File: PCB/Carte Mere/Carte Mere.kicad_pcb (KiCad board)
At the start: 2 copper layers, 62.2 x 23 mm, 40 parts, among them J1 Moteur, J12 Alim 6V, J13 Alim 9V, J2 Moteur, J3 01x20_Female, J4 01x20_Female, J5 IR204, J6 IR204, J7 TL1838, U1 ZXBM5210-S, U2 MC33269DR2-5.0G, U3 ZXBM5210-S, U4 LD1117S33TR_SOT223

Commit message: 1.4 Carte mere
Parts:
- moved J13 57.0 mm to (156.7, 52.5), turned to 90 degrees
- moved J12 41.0 mm to (156.7, 67.8), turned to 90 degrees
- moved J2 1.65 mm to (158.8, 58.8)
- moved J1 0.90 mm to (101.2, 58.7)
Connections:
- J12 pad 1: unconnected-(J12-Pad1) -> /Carte Mere/6V
- J12 pad 2: unconnected-(J12-Pad2) -> GND
- J13 pad 1: unconnected-(J13-Pad1) -> /Carte Mere/9V
- J13 pad 2: unconnected-(J13-Pad2) -> GND
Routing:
- net GND: track 53.0 -> 137.0 mm, vias 0 -> 3
- net /Carte Mere/3.3V: track 4.94 -> 53.7 mm, vias 0 -> 1
- net /Carte Mere/6V: track 12.7 -> 59.6 mm
- net /Carte Mere/9V: track 3.05 -> 48.1 mm
- net /Carte Mere/P2: track 0.00 -> 37.1 mm, vias 0 -> 2
- net Net-(C10-Pad1): track 0.00 -> 29.2 mm, vias 0 -> 2
- net Net-(C11-Pad1): track 0.00 -> 28.7 mm
- net /Carte Mere/P3: track 0.00 -> 27.8 mm
- net Net-(C3-Pad1): track 8.71 -> 34.4 mm, vias 0 -> 2
- net Net-(C4-Pad1): track 9.25 -> 23.2 mm
- net Net-(D3-Pad1): track 0.00 -> 6.43 mm
- net /Carte Mere/5V: track 14.7 -> 20.7 mm
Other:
- board size 62.2 x 23 mm -> 63.5 x 23 mm
- copper layers 2 -> 4
- board text added: "6V"
- board text added: "9V"
- board text added: "GND"

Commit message: 1.6
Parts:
- added J10: Conn_01x04_Male, Connector_PinHeader_2.54mm:PinHeader_1x04_P2.54mm_Vertical, F.Cu at (101.8, 74.0)
- added J11: Conn_01x04_Male, Connector_PinHeader_2.54mm:PinHeader_1x04_P2.54mm_Vertical, F.Cu at (91.5, 99.0)
- added J12: Conn_01x04_Male, Connector_PinHeader_2.54mm:PinHeader_1x04_P2.54mm_Vertical, F.Cu at (91.5, 113.8)
- added J13: Conn_01x04_Male, Connector_PinHeader_2.54mm:PinHeader_1x04_P2.54mm_Vertical, F.Cu at (91.5, 128.0)
- added R10: 10kΩ, Resistor_SMD:R_0805_2012Metric_Pad1.20x1.40mm_HandSolder, F.Cu at (96.8, 134.8)
- added R4: 500Ω, Resistor_SMD:R_0805_2012Metric_Pad1.20x1.40mm_HandSolder, F.Cu at (97.8, 100.5)
- added R5: 500Ω, Resistor_SMD:R_0805_2012Metric_Pad1.20x1.40mm_HandSolder, F.Cu at (97.8, 114.5)
- added R6: 500Ω, Resistor_SMD:R_0805_2012Metric_Pad1.20x1.40mm_HandSolder, F.Cu at (96.8, 129.2)
- added R8: 10kΩ, Resistor_SMD:R_0805_2012Metric_Pad1.20x1.40mm_HandSolder, F.Cu at (97.8, 106.0)
- added R9: 10kΩ, Resistor_SMD:R_0805_2012Metric_Pad1.20x1.40mm_HandSolder, F.Cu at (97.8, 120.2)
- added U5: TCRT5000, Library:tcrt5000, F.Cu at (117.8, 77.6)
- added U6: TCRT5000, Library:tcrt5000, F.Cu at (108.7, 103.3)
- added U7: TCRT5000, Library:tcrt5000, F.Cu at (109.0, 117.4)
- added U8: TCRT5000, Library:tcrt5000, F.Cu at (108.0, 132.1)
- moved R3 80.9 mm to (106.8, 74.8)
- moved R7 70.1 mm to (106.8, 80.2)
- renumbered J12 to J1, J13 to J2, J1 to J3, J2 to J4, J3 to J5, J4 to J6, J5 to J7, J6 to J8, J7 to J9, R9 to R3, R10 to R7
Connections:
- R3 pad 1: unconnected-(R9-Pad1) -> /Capteur/P4
- R7 pad 1: unconnected-(R10-Pad1) -> /Capteur/A0
- R7 pad 2: Net-(J11-Pad2) -> /Capteur/5V
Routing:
- net /Capteur/P4: track 0.00 -> 5.96 mm
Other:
- board size 63.5 x 23 mm -> 63.5 x 39.2 mm

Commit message: Fixed Zach's Stuff
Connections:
- U5 pad 1: (no net) -> Net-(R3-Pad2)
- U5 pad 2: (no net) -> GND
- U5 pad 4: (no net) -> GND
- U6 pad 1: (no net) -> Net-(R4-Pad2)
- U6 pad 2: (no net) -> GND
- U6 pad 3: (no net) -> GND
- U6 pad 4: (no net) -> /Capteur/A0
- U7 pad 1: (no net) -> Net-(R5-Pad2)
- U7 pad 2: (no net) -> GND
- U7 pad 4: (no net) -> GND
- U8 pad 1: (no net) -> Net-(R6-Pad2)
- U8 pad 2: (no net) -> GND
- U8 pad 4: (no net) -> GND
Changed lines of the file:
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@@
     (fp_line (start 1.36 7.59) (end 1.36 3.145) (layer "F.Fab") (width 0.1))
     (fp_line (start -4.14 7.59) (end -4.14 3.145) (layer "F.Fab") (width 0.1))
-    (pad "1" thru_hole oval (at -2.87 6.32 270) (size 1.7 1.7) (drill 1) (layers *.Cu *.Mask))
-    (pad "2" thru_hole rect (at -2.87 3.78 270) (size 1.7 1.7) (drill 1) (layers *.Cu *.Mask))
+    (pad "1" thru_hole oval (at -2.87 6.32 270) (size 1.7 1.7) (drill 1) (layers *.Cu *.Mask)
+      (net 76 "Net-(R6-Pad2)"))
+    (pad "2" thru_hole rect (at -2.87 3.78 270) (size 1.7 1.7) (drill 1) (layers *.Cu *.Mask)
+      (net 2 "GND"))
     (pad "3" thru_hole oval (at 2.63 6.32 270) (size 1.7 1.7) (drill 1) (layers *.Cu *.Mask))
-    (pad "4" thru_hole rect (at 2.63 3.78 270) (size 1.7 1.7) (drill 1) (layers *.Cu *.Mask))
+    (pad "4" thru_hole rect (at 2.63 3.78 270) (size 1.7 1.7) (drill 1) (layers *.Cu *.Mask)
+      (net 2 "GND"))
   )
   (footprint "Library:tcrt5000" (layer "F.Cu")
@@
     (fp_line (start -3.505 2.51) (end -1.6 2.51) (layer "F.Fab") (width 0.1))
     (fp_line (start 3.9 7.59) (end 1.36 7.59) (layer "F.Fab") (width 0.1))
-    (pad "1" thru_hole oval (at -2.87 6.32 270) (size 1.7 1.7) (drill 1) (layers *.Cu *.Mask))
-    (pad "2" thru_hole rect (at -2.87 3.78 270) (size 1.7 1.7) (drill 1) (layers *.Cu *.Mask))
+    (pad "1" thru_hole oval (at -2.87 6.32 270) (size 1.7 1.7) (drill 1) (layers *.Cu *.Mask)
+      (net 32 "Net-(R3-Pad2)"))
+    (pad "2" thru_hole rect (at -2.87 3.78 270) (size 1.7 1.7) (drill 1) (layers *.Cu *.Mask)
+      (net 2 "GND"))
     (pad "3" thru_hole oval (at 2.63 6.32 270) (size 1.7 1.7) (drill 1) (layers *.Cu *.Mask))
-    (pad "4" thru_hole rect (at 2.63 3.78 270) (size 1.7 1.7) (drill 1) (layers *.Cu *.Mask))
+    (pad "4" thru_hole rect (at 2.63 3.78 270) (size 1.7 1.7) (drill 1) (layers *.Cu *.Mask)
+      (net 2 "GND"))
   )
   (footprint "Resistor_SMD:R_0805_2012Metric_Pad1.20x1.40mm_HandSolder" (layer "F.Cu")
@@
     (fp_line (start -1.6 7.59) (end -4.14 7.59) (layer "F.Fab") (width 0.1))
     (fp_line (start 1.36 7.59) (end 1.36 3.145) (layer "F.Fab") (width 0.1))
-    (pad "1" thru_hole oval (at -2.87 6.32 270) (size 1.7 1.7) (drill 1) (layers *.Cu *.Mask))
-    (pad "2" thru_hole rect (at -2.87 3.78 270) (size 1.7 1.7) (drill 1) (layers *.Cu *.Mask))
-    (pad "3" thru_hole oval (at 2.63 6.32 270) (size 1.7 1.7) (drill 1) (layers *.Cu *.Mask))
-    (pad "4" thru_hole rect (at 2.63 3.78 270) (size 1.7 1.7) (drill 1) (layers *.Cu *.Mask))
+    (pad "1" thru_hole oval (at -2.87 6.32 270) (size 1.7 1.7) (drill 1) (layers *.Cu *.Mask)
+      (net 34 "Net-(R4-Pad2)"))
+    (pad "2" thru_hole rect (at -2.87 3.78 270) (size 1.7 1.7) (drill 1) (layers *.Cu *.Mask)
+      (net 2 "GND"))
+    (pad "3" thru_hole rect (at 2.63 3.78 270) (size 1.7 1.7) (drill 1) (layers *.Cu *.Mask)
+      (net 2 "GND"))
+    (pad "4" thru_hole oval (at 2.63 6.32 270) (size 1.7 1.7) (drill 1) (layers *.Cu *.Mask)
+      (net 67 "/Capteur/A0"))
   )
   (footprint "Resistor_SMD:R_0805_2012Metric_Pad1.20x1.40mm_HandSolder" (layer "F.Cu")
@@
     (fp_line (start -4.14 3.145) (end -3.505 2.51) (layer "F.Fab") (width 0.1))
     (fp_line (start -4.14 7.59) (end -4.14 3.145) (layer "F.Fab") (width 0.1))
-    (pad "1" thru_hole oval (at -2.87 6.32 270) (size 1.7 1.7) (drill 1) (layers *.Cu *.Mask))
-    (pad "2" thru_hole rect (at -2.87 3.78 270) (size 1.7 1.7) (drill 1) (layers *.Cu *.Mask))
+    (pad "1" thru_hole oval (at -2.87 6.32 270) (size 1.7 1.7) (drill 1) (layers *.Cu *.Mask)
+      (net 66 "Net-(R5-Pad2)"))
+    (pad "2" thru_hole rect (at -2.87 3.78 270) (size 1.7 1.7) (drill 1) (layers *.Cu *.Mask)
+      (net 2 "GND"))
     (pad "3" thru_hole oval (at 2.63 6.32 270) (size 1.7 1.7) (drill 1) (layers *.Cu *.Mask))
-    (pad "4" thru_hole rect (at 2.63 3.78 270) (size 1.7 1.7) (drill 1) (layers *.Cu *.Mask))
+    (pad "4" thru_hole rect (at 2.63 3.78 270) (size 1.7 1.7) (drill 1) (layers *.Cu *.Mask)
+      (net 2 "GND"))
   )
   (footprint "Resistor_SMD:R_0805_2012Metric_Pad1.20x1.40mm_HandSolder" (layer "F.Cu")

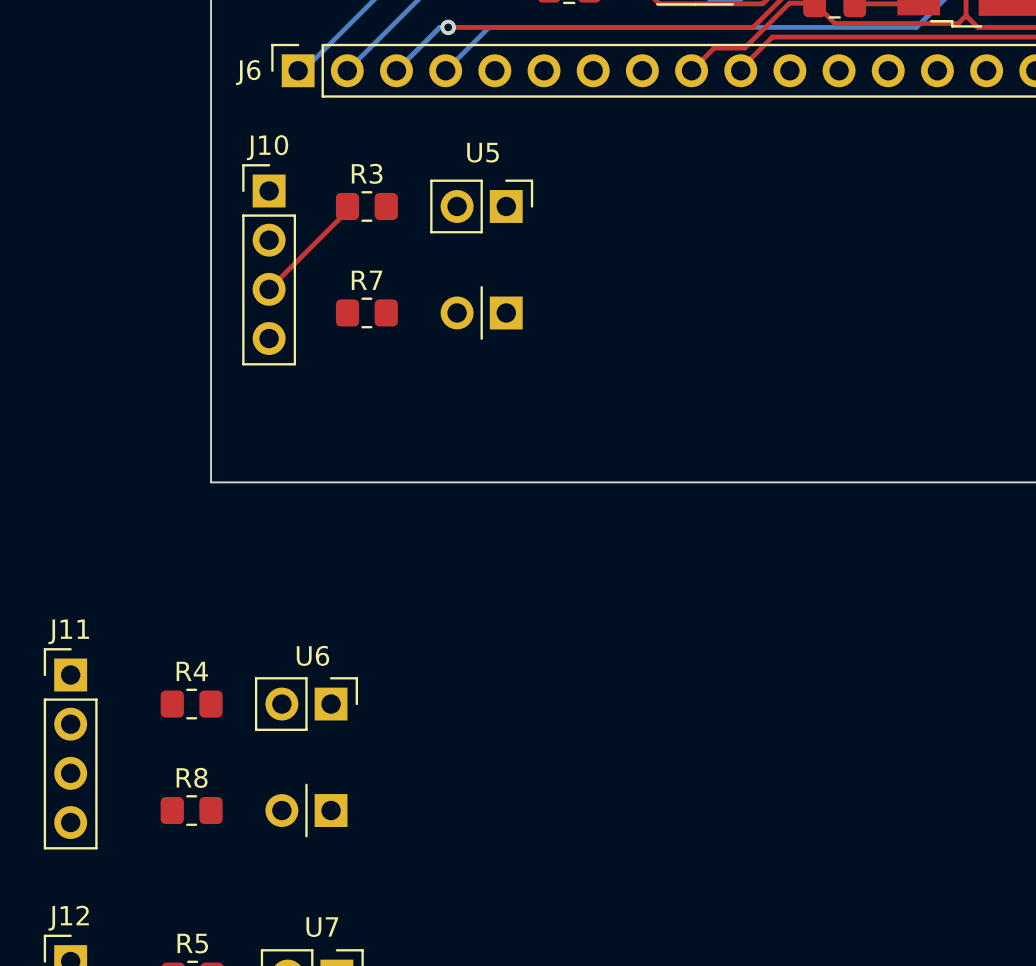
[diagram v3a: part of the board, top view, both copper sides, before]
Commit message: added lib for tcrt5000
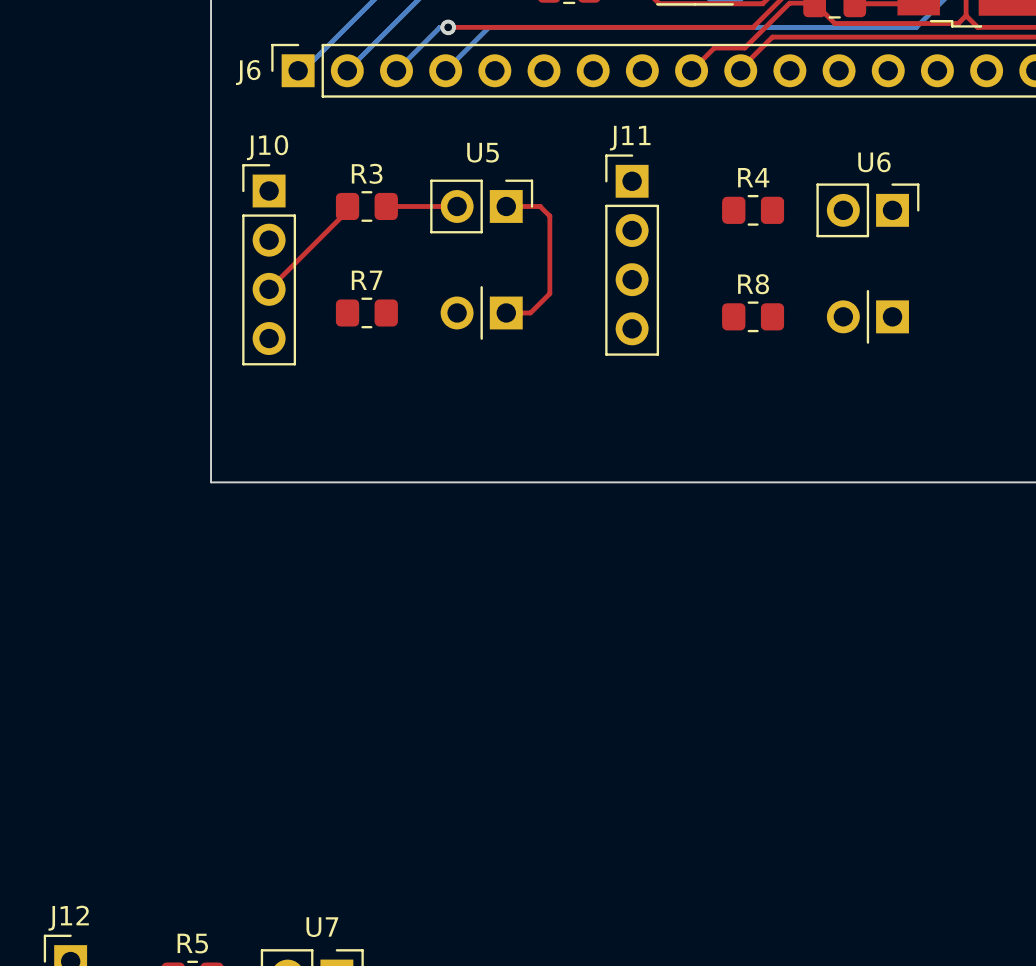
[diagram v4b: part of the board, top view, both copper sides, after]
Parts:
- moved J11 38.6 mm to (120.5, 73.5)
- moved R4 38.6 mm to (126.8, 75.0)
- moved R8 38.6 mm to (126.8, 80.5)
- moved U6 38.6 mm to (137.7, 77.8)
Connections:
- J11 pad 4: /Capteur/A0 -> /Capteur/A1
- J12 pad 4: /Capteur/A0 -> /Capteur/A2
- J13 pad 4: /Capteur/A0 -> /Capteur/A3
- R10 pad 1: /Capteur/A0 -> /Capteur/A3
- R8 pad 1: /Capteur/A0 -> /Capteur/A1
- R9 pad 1: /Capteur/A0 -> /Capteur/A2
- U5 pad 1: Net-(R3-Pad2) -> (no net)
- U5 pad 2: GND -> (no net)
- U5 pad 4: GND -> (no net)
- U6 pad 1: Net-(R4-Pad2) -> (no net)
- U6 pad 2: GND -> (no net)
- U6 pad 3: GND -> (no net)
- U6 pad 4: /Capteur/A0 -> (no net)
- U7 pad 1: Net-(R5-Pad2) -> (no net)
- U7 pad 2: GND -> (no net)
- U7 pad 4: GND -> (no net)
- U8 pad 1: Net-(R6-Pad2) -> (no net)
- U8 pad 2: GND -> (no net)
- U8 pad 4: GND -> (no net)
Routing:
- net GND: track 137.0 -> 146.1 mm
- net Net-(R3-Pad2): track 0.00 -> 3.66 mm

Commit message: 1.9
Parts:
- U5, U6, U7, U8: footprint Library:tcrt5000 -> Sumo:OPTO_TCRT5000
- moved U7 14.7 mm to (106.0, 131.8), turned to 90 degrees
- moved R10 14.6 mm to (98.8, 149.2)
- moved R6 14.6 mm to (98.8, 143.8)
- moved J12 14.6 mm to (93.0, 128.2)
- moved J13 14.6 mm to (93.0, 142.4)
- moved R5 14.5 mm to (98.8, 129.0)
- moved R9 14.5 mm to (98.8, 134.8)
- moved U8 14.5 mm to (106.0, 146.5), turned to 90 degrees
- moved J11 3.56 mm to (124.0, 74.2)
- moved R4 3.07 mm to (129.7, 75.7)
- moved R8 3.07 mm to (129.7, 81.2)
- moved U5 2.53 mm to (115.2, 77.8), turned to 90 degrees
- moved R3 1.21 mm to (108.0, 75.0)
- moved R7 1.21 mm to (108.0, 80.5)
- moved U6 0.85 mm to (137.0, 78.2), turned to 90 degrees
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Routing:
- net GND: track 146.1 -> 137.0 mm
- net /Capteur/P4: track 5.96 -> 0.00 mm
- net Net-(R3-Pad2): track 3.66 -> 0.00 mm

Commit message: 2.0 alabama
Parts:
- removed J7, J8: IR204, LED_THT:LED_D1.8mm_W1.8mm_H2.4mm_Horizontal_O6.35mm_Z8.2mm
- removed the R3 at (171.8, 119.9)
- removed the R4 at (164.5, 126.2)
- removed the R5 at (174.0, 125.8)
- removed the R6 at (169.2, 126.2)
- removed the R7 at (180.0, 114.2)
- removed the R8 at (176.6, 119.9)
- added J14: 01x20_Female, Connector_PinSocket_2.54mm:PinSocket_1x20_P2.54mm_Vertical, F.Cu at (103.2, 48.8)
- added J15: 01x20_Female, Connector_PinSocket_2.54mm:PinSocket_1x20_P2.54mm_Vertical, F.Cu at (103.2, 71.5)
- J9: footprint Package_TO_SOT_THT:TO-92L_Inline_Wide -> Connector_PinHeader_2.54mm:PinHeader_1x03_P2.54mm_Vertical
- moved J12 72.4 mm to (144.7, 77.5)
- moved R5 72.4 mm to (150.4, 78.2)
- moved R9 72.4 mm to (150.4, 84.0), turned to 180 degrees
- moved U7 72.4 mm to (157.7, 81.0)
- moved R10 52.8 mm to (108.0, 97.2), turned to 180 degrees
- moved R6 52.8 mm to (108.0, 91.8)
- moved U8 52.8 mm to (115.2, 94.5)
- moved J13 52.8 mm to (102.2, 90.5)
- moved J10 3.00 mm to (102.2, 77.2)
- moved J11 3.00 mm to (124.0, 77.2)
- moved R3 3.00 mm to (108.0, 78.0)
- moved R4 3.00 mm to (129.7, 78.7)
- moved R7 3.00 mm to (108.0, 83.5), turned to 180 degrees
- moved R8 3.00 mm to (129.7, 84.2), turned to 180 degrees
- moved U5 3.00 mm to (115.2, 80.8)
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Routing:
- net GND: track 137.0 -> 252.6 mm, vias 3 -> 5
- net /Capteur/5V: track 0.00 -> 49.7 mm
- net /Capteur/A1: track 0.00 -> 12.8 mm
- net /Capteur/A3: track 0.00 -> 12.8 mm
- net /Capteur/A2: track 0.00 -> 12.3 mm
- net /Capteur/A0: track 0.00 -> 12.3 mm
- net /Carte Mere/3.3V: track 53.7 -> 60.9 mm
- net /Capteur/P6: track 0.00 -> 6.54 mm
- net /Capteur/P4: track 0.00 -> 6.52 mm
- net /Capteur/P7: track 0.00 -> 6.32 mm
- net /Capteur/P5: track 0.00 -> 6.23 mm
- net Net-(R4-Pad2): track 0.00 -> 5.08 mm
- net Net-(R3-Pad2): track 0.00 -> 5.00 mm
- net Net-(R6-Pad2): track 0.00 -> 4.98 mm
- net Net-(R5-Pad2): track 0.00 -> 4.98 mm
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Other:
- board size 63.5 x 39.2 mm -> 63.5 x 60 mm
- board text added: "5V"
- board text added: "A0"
- board text added: "A1"
- board text added: "A2"
- board text added: "A3"

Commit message: 2.1 Missouri
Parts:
- removed R10, R9: 10kΩ, Resistor_SMD:R_0805_2012Metric_Pad1.20x1.40mm_HandSolder
- added C13: 100uf, Capacitor_SMD:C_0805_2012Metric_Pad1.18x1.45mm_HandSolder, B.Cu at (172.9, 78.8)
- added J16: Conn_01x03_Male, Connector_PinHeader_2.54mm:PinHeader_1x03_P2.54mm_Vertical, F.Cu at (123.5, 75.5)
- added J17: Conn_01x03_Male, Connector_PinHeader_2.54mm:PinHeader_1x03_P2.54mm_Vertical, F.Cu at (133.7, 75.5)
- added J7: Conn_01x03_Male, Connector_PinHeader_2.54mm:PinHeader_1x03_P2.54mm_Vertical, F.Cu at (101.7, 83.5)
- added J8: Conn_01x03_Male, Connector_PinHeader_2.54mm:PinHeader_1x03_P2.54mm_Vertical, F.Cu at (124.9, 83.5)
- added RV1: 100k, Potentiometer_THT:Potentiometer_ACP_CA6-H2,5_Horizontal, F.Cu at (106.3, 87.0)
- added RV2: 100k, Potentiometer_THT:Potentiometer_ACP_CA6-H2,5_Horizontal, F.Cu at (129.6, 86.8)
- added RV3: 100k, Potentiometer_THT:Potentiometer_ACP_CA6-H2,5_Horizontal, F.Cu at (106.4, 102.0)
- added RV4: 100k, Potentiometer_THT:Potentiometer_ACP_CA6-H2,5_Horizontal, F.Cu at (129.7, 102.2)
- J10, J11, J12, J13: value Conn_01x04_Male -> Conn_01x03_Male; footprint Connector_PinHeader_2.54mm:PinHeader_1x04_P2.54mm_Vertical -> Connector_PinHeader_2.54mm:PinHeader_1x03_P2.54mm_Vertical
- R7: value 10kΩ -> 100Ω
- R8: value 10kΩ -> 20kΩ
- moved R7 63.1 mm to (170.9, 78.8), turned to 0 degrees
- moved R5 47.4 mm to (107.7, 98.8)
- moved U7 47.4 mm to (115.0, 101.5)
- moved R8 45.5 mm to (174.9, 78.8)
- moved J12 41.4 mm to (103.2, 75.5), turned to 90 degrees
- moved J9 40.2 mm to (169.9, 75.8), turned to 90 degrees
- moved R6 23.9 mm to (130.9, 98.8)
- moved U8 23.9 mm to (138.2, 101.5)
- moved J11 21.6 mm to (124.9, 98.8)
- moved J10 21.6 mm to (101.7, 98.8)
- moved J13 18.7 mm to (113.5, 75.5), turned to 90 degrees
- moved R3 5.52 mm to (107.5, 83.5)
- moved U5 5.52 mm to (114.8, 86.2)
- moved R4 4.86 mm to (130.8, 83.5)
- moved U6 4.86 mm to (138.1, 86.0)
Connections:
- J10 pad 1: /Capteur/5V -> /Capteur/3.3V
- J10 pad 3: /Capteur/P4 -> /Capteur/A2
- J11 pad 1: /Capteur/5V -> /Capteur/3.3V
- J11 pad 3: /Capteur/P5 -> /Capteur/A3
- J12 pad 1: /Capteur/5V -> /Carte Mere/3.3V
- J12 pad 3: /Capteur/P6 -> /Carte Mere/P4
- J13 pad 1: /Capteur/5V -> /Carte Mere/3.3V
- J13 pad 3: /Capteur/P7 -> /Carte Mere/P5
- J9 pad 1: unconnected-(J9-Pad1) -> Net-(J9-Pad1)
- J9 pad 2: unconnected-(J9-Pad2) -> GND
- J9 pad 3: unconnected-(J9-Pad3) -> Net-(J9-Pad3)
- R3 pad 1: /Capteur/P4 -> /Capteur/3.3V
- R4 pad 1: /Capteur/P5 -> /Capteur/3.3V
- R5 pad 1: /Capteur/P6 -> /Capteur/3.3V
- R6 pad 1: /Capteur/P7 -> /Capteur/3.3V
- R7 pad 1: /Capteur/A0 -> Net-(J9-Pad1)
- R7 pad 2: /Capteur/5V -> Net-(C13-Pad2)
- R8 pad 1: /Capteur/A1 -> Net-(J9-Pad3)
- R8 pad 2: /Capteur/5V -> Net-(C13-Pad2)
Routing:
- net /Capteur/3.3V: track 0.00 -> 74.9 mm
- net /Capteur/5V: track 49.7 -> 0.00 mm
- net GND: track 252.6 -> 297.6 mm
- net /Carte Mere/3.3V: track 60.9 -> 99.4 mm
- net /Carte Mere/P7: track 3.76 -> 23.2 mm
- net /Carte Mere/P6: track 3.76 -> 15.5 mm
- net /Carte Mere/P4: track 3.76 -> 10.5 mm
- net /Capteur/P6: track 6.54 -> 0.00 mm
- net /Capteur/P4: track 6.52 -> 0.00 mm
- net /Capteur/P7: track 6.32 -> 0.00 mm
- net /Capteur/P5: track 6.23 -> 0.00 mm
- net Net-(C13-Pad2): track 0.00 -> 5.34 mm, vias 0 -> 1
- net /Carte Mere/P5: track 3.76 -> 8.84 mm
- net Net-(J9-Pad3): track 0.00 -> 3.39 mm
- net Net-(J9-Pad1): track 0.00 -> 3.01 mm
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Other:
- board size 63.5 x 60 mm -> 63.5 x 62.2 mm
- board text added: "3.3V"
- board text added: "OUT1"
- board text added: "OUT2"
- board text added: "TL1838"

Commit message: 2.2 Florida
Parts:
- J12, J13, J16, J17: value Conn_01x03_Male -> Conn_Tcrt5000
- moved C13 17.1 mm to (157.2, 72.0), turned to 180 degrees
- moved J9 16.9 mm to (153.0, 75.8)
- moved R7 16.9 mm to (155.5, 72.0)
- moved R8 16.9 mm to (159.5, 72.0)
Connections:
- C12 pad 1: /Carte Mere/3.3V -> 3.3V
- C13 pad 2: Net-(C13-Pad2) -> 3.3V
- J10 pad 1: /Capteur/3.3V -> 3.3V
- J11 pad 1: /Capteur/3.3V -> 3.3V
- J12 pad 1: /Carte Mere/3.3V -> 3.3V
- J13 pad 1: /Carte Mere/3.3V -> 3.3V
- J14 pad 9: /Carte Mere/3.3V -> 3.3V
- J15 pad 10: /Carte Mere/3.3V -> 3.3V
- J15 pad 13: /Carte Mere/P8 -> P8
- J16 pad 1: /Carte Mere/3.3V -> 3.3V
- J17 pad 1: /Carte Mere/3.3V -> 3.3V
- J5 pad 9: /Carte Mere/3.3V -> 3.3V
- J6 pad 10: /Carte Mere/3.3V -> 3.3V
- J6 pad 13: /Carte Mere/P8 -> P8
- J7 pad 1: /Capteur/3.3V -> 3.3V
- J8 pad 1: /Capteur/3.3V -> 3.3V
- J9 pad 3: Net-(J9-Pad3) -> P8
- R3 pad 1: /Capteur/3.3V -> 3.3V
- R4 pad 1: /Capteur/3.3V -> 3.3V
- R5 pad 1: /Capteur/3.3V -> 3.3V
- R6 pad 1: /Capteur/3.3V -> 3.3V
- R7 pad 2: Net-(C13-Pad2) -> 3.3V
- R8 pad 1: Net-(J9-Pad3) -> P8
- R8 pad 2: Net-(C13-Pad2) -> 3.3V
- RV1 pad 1: /Capteur/3.3V -> 3.3V
- RV1 pad 2: /Capteur/3.3V -> 3.3V
- RV2 pad 1: /Capteur/3.3V -> 3.3V
- RV2 pad 2: /Capteur/3.3V -> 3.3V
- RV3 pad 1: /Capteur/3.3V -> 3.3V
- RV3 pad 2: /Capteur/3.3V -> 3.3V
- RV4 pad 1: /Capteur/3.3V -> 3.3V
- RV4 pad 2: /Capteur/3.3V -> 3.3V
- U4 pad 2: /Carte Mere/3.3V -> 3.3V
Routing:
- net 3.3V: track 0.00 -> 203.8 mm, vias 0 -> 2
- net /Carte Mere/3.3V: track 99.4 -> 0.00 mm, vias 1 -> 0
- net /Capteur/3.3V: track 74.9 -> 0.00 mm
- net P8: track 0.00 -> 36.4 mm
- net GND: track 297.6 -> 303.9 mm
- net Net-(C13-Pad2): track 5.34 -> 0.00 mm, vias 1 -> 0
- net /Carte Mere/P8: track 3.76 -> 0.00 mm
- net Net-(J9-Pad3): track 3.39 -> 0.00 mm
- net Net-(J9-Pad1): track 3.01 -> 4.38 mm
